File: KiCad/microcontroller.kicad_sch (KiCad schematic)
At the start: 11 parts, among them J1 Debugger, SW1 Reset switch, U1 STM32F051C6Tx, U7 24LC256

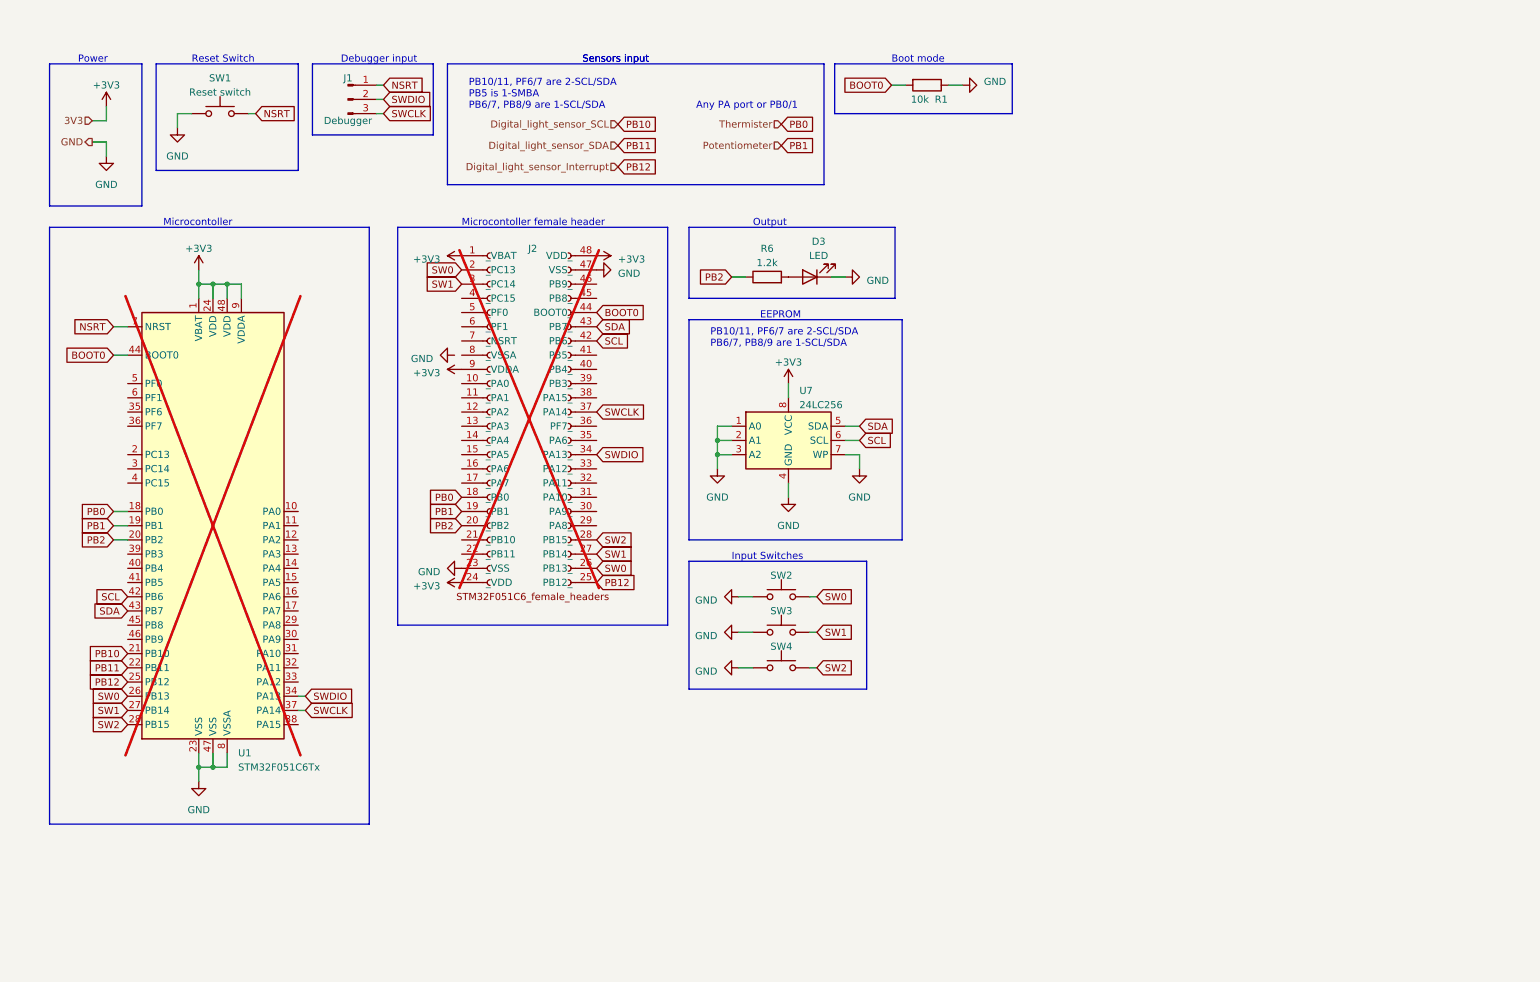
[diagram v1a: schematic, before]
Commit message: added USB to UART connector and made a dedicated USB sheet
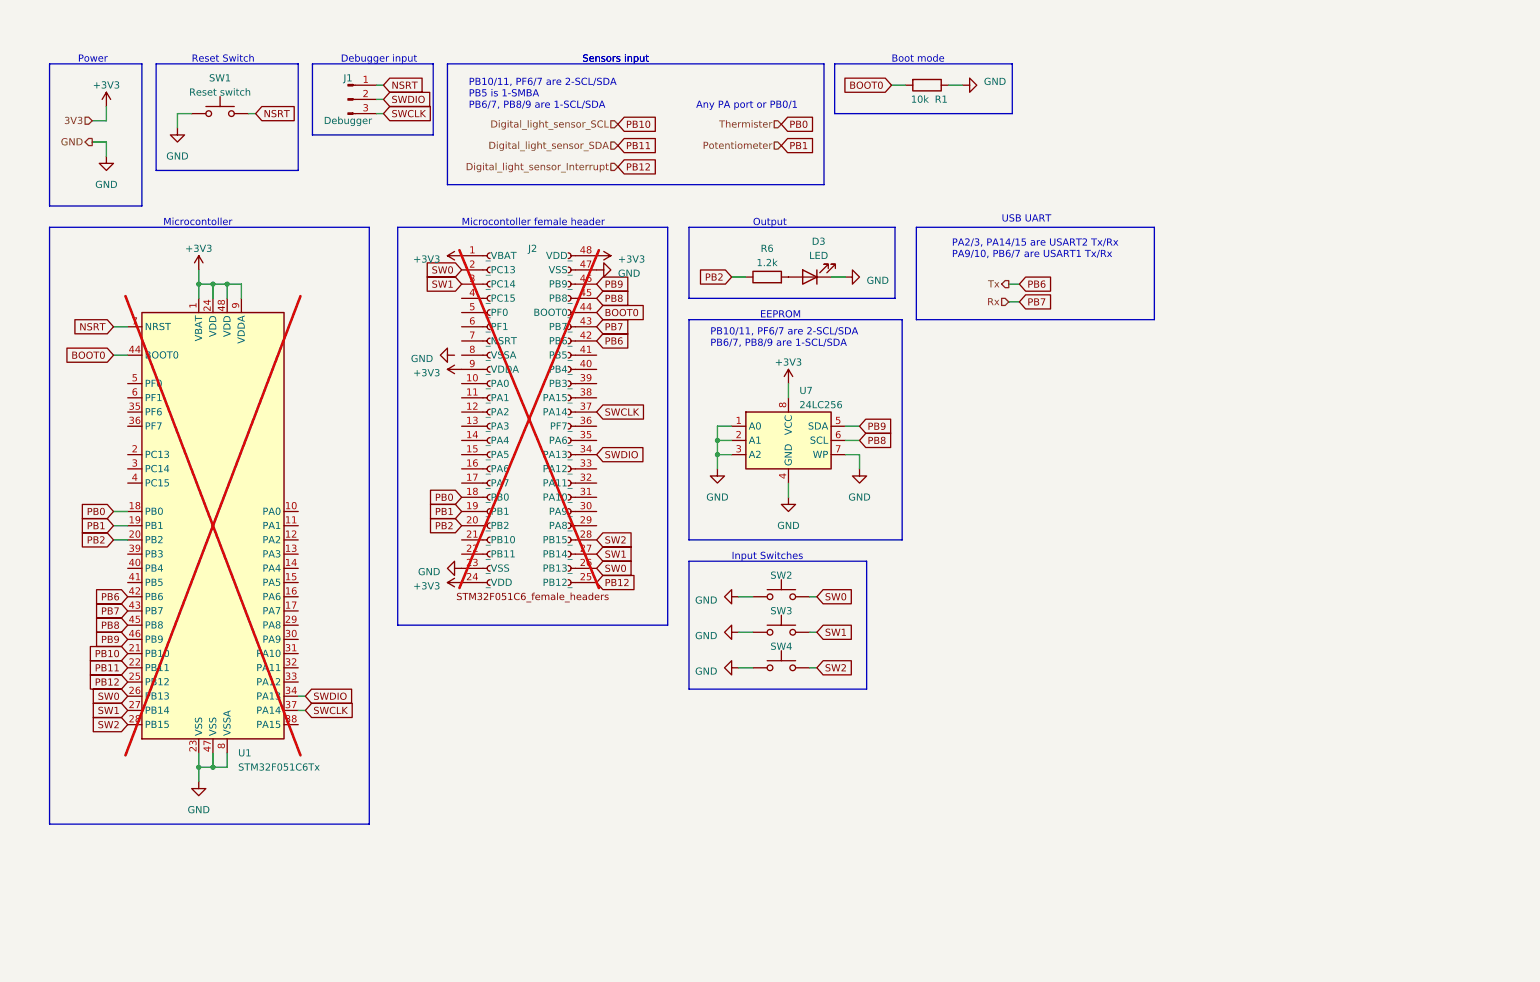
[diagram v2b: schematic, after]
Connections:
- net PB8: now reaches J2.45 (PB8_)
- net PB8: now also U1.45 (PB8), U7.6 (SCL)
- net PB9: now reaches J2.46 (PB9_)
- net PB9: now also U1.46 (PB9), U7.5 (SDA)
- net SCL renamed PB6
- net PB6: no longer U7.6 (SCL)
- net SDA renamed PB7
- net PB7: no longer U7.5 (SDA)
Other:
- note added: "PA2/3, PA14/15 are USART2 Tx/Rx PA9/10, PB6/7 are USART1 Tx/Rx"
- note added: "USB UART"
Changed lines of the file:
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@@
+    (stroke (width 0) (type default))
+  )
+  (wire (pts (xy 190.5 60.96) (xy 192.405 60.96))
     (stroke (width 0) (type default))
   )
@@
     (stroke (width 0) (type default))
   )
+  (wire (pts (xy 190.5 64.135) (xy 192.405 64.135))
+    (stroke (width 0) (type default))
+  )
   (wire (pts (xy 138.43 91.44) (xy 138.43 93.98))
     (stroke (width 0) (type default))
@@
     (fill (type none))
   )
+  (rectangle (start 173.99 50.8) (end 216.535 67.31)
+    (stroke (width 0) (type default))
+    (fill (type none))
+  )
   (rectangle (start 19.05 21.59) (end 35.56 46.99)
     (stroke (width 0) (type default))
@@
     (effects (font (size 1.27 1.27)) (justify left bottom))
   )
+  (text "PA2/3, PA14/15 are USART2 Tx/Rx\nPA9/10, PB6/7 are USART1 Tx/Rx"
+    (at 180.34 56.515 0)
+    (effects (font (size 1.27 1.27)) (justify left bottom))
+  )
   (text "EEPROM" (at 146.05 67.31 0)
     (effects (font (size 1.27 1.27)) (justify left bottom))
   )
   (text "Boot mode" (at 169.545 21.59 0)
+    (effects (font (size 1.27 1.27)) (justify left bottom))
+  )
+  (text "USB UART" (at 189.23 50.165 0)
     (effects (font (size 1.27 1.27)) (justify left bottom))
   )
@@
     (effects (font (size 1.27 1.27)) (justify left bottom))
   )
+  (global_label "PB6" (shape input) (at 192.405 60.96 0) (fields_autoplaced)
+    (effects (font (size 1.27 1.27)) (justify left))
+    (property "Intersheetrefs" "${INTERSHEET_REFS}" (at 199.0603 60.96 0)
+      (effects (font (size 1.27 1.27)) (justify left) hide)
+    )
+  )
   (global_label "PB1" (shape input) (at 149.86 36.195 0) (fields_autoplaced)
     (effects (font (size 1.27 1.27)) (justify left))
@@
     )
   )
-  (global_label "SDA" (shape input) (at 163.83 86.36 0) (fields_autoplaced)
-    (effects (font (size 1.27 1.27)) (justify left))
-    (property "Intersheetrefs" "${INTERSHEET_REFS}" (at 170.3039 86.36 0)
-      (effects (font (size 1.27 1.27)) (justify left) hide)
+  (global_label "PB9" (shape input) (at 163.83 86.36 0) (fields_autoplaced)
+    (effects (font (size 1.27 1.27)) (justify left))
+    (property "Intersheetrefs" "${INTERSHEET_REFS}" (at 170.4853 86.36 0)
+      (effects (font (size 1.27 1.27)) (justify left) hide)
+    )
+  )
+  (global_label "PB9" (shape input) (at 33.02 124.46 180) (fields_autoplaced)
+    (effects (font (size 1.27 1.27)) (justify right))
+    (property "Intersheetrefs" "${INTERSHEET_REFS}" (at 26.3647 124.46 0)
+      (effects (font (size 1.27 1.27)) (justify right) hide)
     )
   )
@@
     )
   )
-  (global_label "SCL" (shape input) (at 163.83 88.9 0) (fields_autoplaced)
-    (effects (font (size 1.27 1.27)) (justify left))
-    (property "Intersheetrefs" "${INTERSHEET_REFS}" (at 170.2434 88.9 0)
+  (global_label "PB8" (shape input) (at 163.83 88.9 0) (fields_autoplaced)
+    (effects (font (size 1.27 1.27)) (justify left))
+    (property "Intersheetrefs" "${INTERSHEET_REFS}" (at 170.4853 88.9 0)
       (effects (font (size 1.27 1.27)) (justify left) hide)
     )
@@
     )
   )
-  (global_label "SCL" (shape input) (at 33.02 116.84 180) (fields_autoplaced)
-    (effects (font (size 1.27 1.27)) (justify right))
-    (property "Intersheetrefs" "${INTERSHEET_REFS}" (at 26.6066 116.84 0)
-      (effects (font (size 1.27 1.27)) (justify right) hide)
-    )
-  )
-  (global_label "SCL" (shape input) (at 116.84 71.12 0) (fields_autoplaced)
-    (effects (font (size 1.27 1.27)) (justify left))
-    (property "Intersheetrefs" "${INTERSHEET_REFS}" (at 123.2534 71.12 0)
+  (global_label "PB6" (shape input) (at 33.02 116.84 180) (fields_autoplaced)
+    (effects (font (size 1.27 1.27)) (justify right))
+    (property "Intersheetrefs" "${INTERSHEET_REFS}" (at 26.3647 116.84 0)
+      (effects (font (size 1.27 1.27)) (justify right) hide)
+    )
+  )
+  (global_label "PB6" (shape input) (at 116.84 71.12 0) (fields_autoplaced)
+    (effects (font (size 1.27 1.27)) (justify left))
+    (property "Intersheetrefs" "${INTERSHEET_REFS}" (at 123.4953 71.12 0)
       (effects (font (size 1.27 1.27)) (justify left) hide)
     )
@@
     )
   )
-  (global_label "SDA" (shape input) (at 33.02 119.38 180) (fields_autoplaced)
-    (effects (font (size 1.27 1.27)) (justify right))
-    (property "Intersheetrefs" "${INTERSHEET_REFS}" (at 26.5461 119.38 0)
+  (global_label "PB7" (shape input) (at 33.02 119.38 180) (fields_autoplaced)
+    (effects (font (size 1.27 1.27)) (justify right))
+    (property "Intersheetrefs" "${INTERSHEET_REFS}" (at 26.3647 119.38 0)
       (effects (font (size 1.27 1.27)) (justify right) hide)
     )
@@
     )
   )
+  (global_label "PB7" (shape input) (at 192.405 64.135 0) (fields_autoplaced)
+    (effects (font (size 1.27 1.27)) (justify left))
+    (property "Intersheetrefs" "${INTERSHEET_REFS}" (at 199.0603 64.135 0)
+      (effects (font (size 1.27 1.27)) (justify left) hide)
+    )
+  )
   (global_label "SWCLK" (shape input) (at 78.74 30.48 0) (fields_autoplaced)
     (effects (font (size 1.27 1.27)) (justify left))
@@
     )
   )
+  (global_label "PB8" (shape input) (at 116.84 63.5 0) (fields_autoplaced)
+    (effects (font (size 1.27 1.27)) (justify left))
+    (property "Intersheetrefs" "${INTERSHEET_REFS}" (at 123.4953 63.5 0)
+      (effects (font (size 1.27 1.27)) (justify left) hide)
+    )
+  )
+  (global_label "PB9" (shape input) (at 116.84 60.96 0) (fields_autoplaced)
+    (effects (font (size 1.27 1.27)) (justify left))
+    (property "Intersheetrefs" "${INTERSHEET_REFS}" (at 123.4953 60.96 0)
+      (effects (font (size 1.27 1.27)) (justify left) hide)
+    )
+  )
   (global_label "SWCLK" (shape input) (at 116.84 83.82 0) (fields_autoplaced)
     (effects (font (size 1.27 1.27)) (justify left))
@@
     )
   )
-  (global_label "SDA" (shape input) (at 116.84 68.58 0) (fields_autoplaced)
-    (effects (font (size 1.27 1.27)) (justify left))
-    (property "Intersheetrefs" "${INTERSHEET_REFS}" (at 123.3139 68.58 0)
+  (global_label "PB7" (shape input) (at 116.84 68.58 0) (fields_autoplaced)
+    (effects (font (size 1.27 1.27)) (justify left))
+    (property "Intersheetrefs" "${INTERSHEET_REFS}" (at 123.4953 68.58 0)
       (effects (font (size 1.27 1.27)) (justify left) hide)
     )
@@
     )
   )
+  (global_label "PB8" (shape input) (at 33.02 121.92 180) (fields_autoplaced)
+    (effects (font (size 1.27 1.27)) (justify right))
+    (property "Intersheetrefs" "${INTERSHEET_REFS}" (at 26.3647 121.92 0)
+      (effects (font (size 1.27 1.27)) (justify right) hide)
+    )
+  )
   (global_label "SW2" (shape input) (at 156.21 129.54 0) (fields_autoplaced)
     (effects (font (size 1.27 1.27)) (justify left))
@@
     )
   )
+  (hierarchical_label "Rx" (shape input) (at 190.5 64.135 180) (fields_autoplaced)
+    (effects (font (size 1.27 1.27)) (justify right))
+  )
   (hierarchical_label "Digital_light_sensor_SCL" (shape input) (at 120.65 32.385 180) (fields_autoplaced)
     (effects (font (size 1.27 1.27)) (justify right))
@@
     (effects (font (size 1.27 1.27)) (justify right))
   )
+  (hierarchical_label "Tx" (shape output) (at 190.5 60.96 180) (fields_autoplaced)
+    (effects (font (size 1.27 1.27)) (justify right))
+  )

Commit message: Added sheet notes and initial design template, reordered microcontoller subsheet and add microntoller subsheet notes
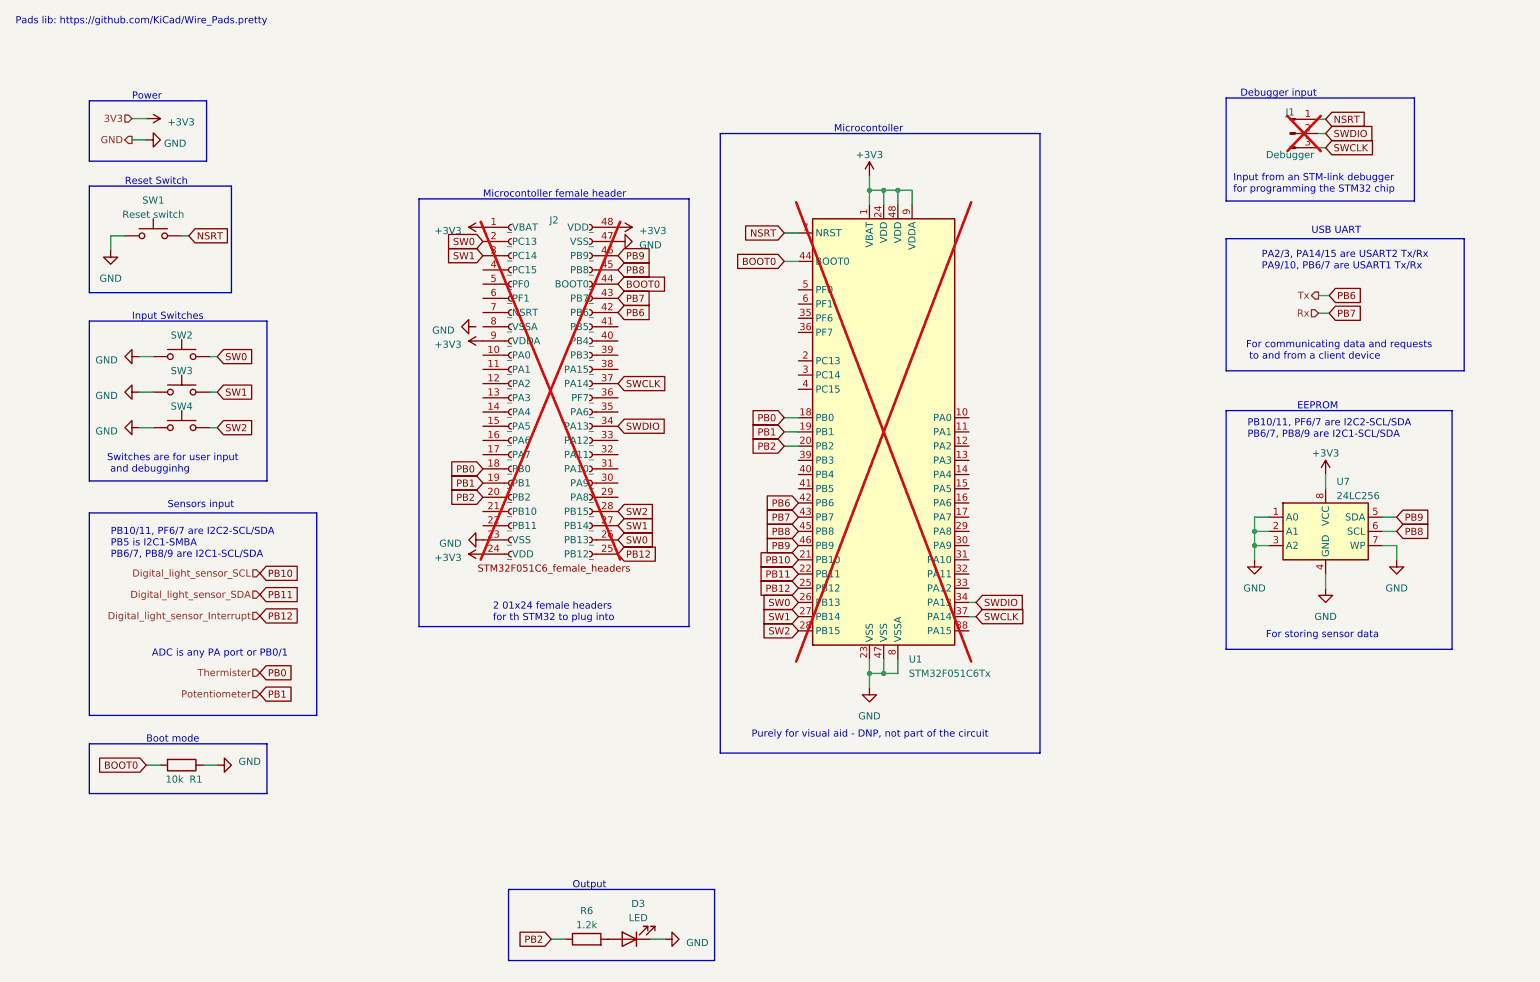
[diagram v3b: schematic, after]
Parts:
- J1: now not fitted
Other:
- note added: "2 01x24 female headers for th STM32 to plug into"
- note added: "ADC is any PA port or PB0/1"
- note added: "For communicating data and requests to and from a client device"
- note added: "For storing sensor data"
- note added: "Input from an STM-link debugger for programming the STM32 chip"
- note added: "PB10/11, PF6/7 are I2C2-SCL/SDA PB5 is I2C1-SMBA PB6/7, PB8/9 are I2C1-SCL/SDA"
- note added: "PB10/11, PF6/7 are I2C2-SCL/SDA PB6/7, PB8/9 are I2C1-SCL/SDA"
- note added: "Pads lib: https://github.com/KiCad/Wire_Pads.pretty"
- note added: "Purely for visual aid - DNP, not part of the circuit"
- note added: "Switches are for user input and debugginhg"
- note removed: "Any PA port or PB0/1"
- note removed: "PB10/11, PF6/7 are 2-SCL/SDA PB5 is 1-SMBA PB6/7, PB8/9 are 1-SCL/SDA"
- note removed: "PB10/11, PF6/7 are 2-SCL/SDA PB6/7, PB8/9 are 1-SCL/SDA"
- company: (none) -> UCT
- title: (none) -> Microcontoller subsystem
- moved on the sheet: D3, J2, R1, R6, SW1, SW2, SW3, SW4, U1, U7
